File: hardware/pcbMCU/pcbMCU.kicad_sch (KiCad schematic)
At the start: 30 parts, among them J1 Conn_01x02, J2 Conn_01x04, J3 Conn_01x03, J4 Conn_01x05, SW1 SW_SPDT, U1 AMS1117-3.3, U2 AP62300, U3 ESP32-S3-WROOM-1

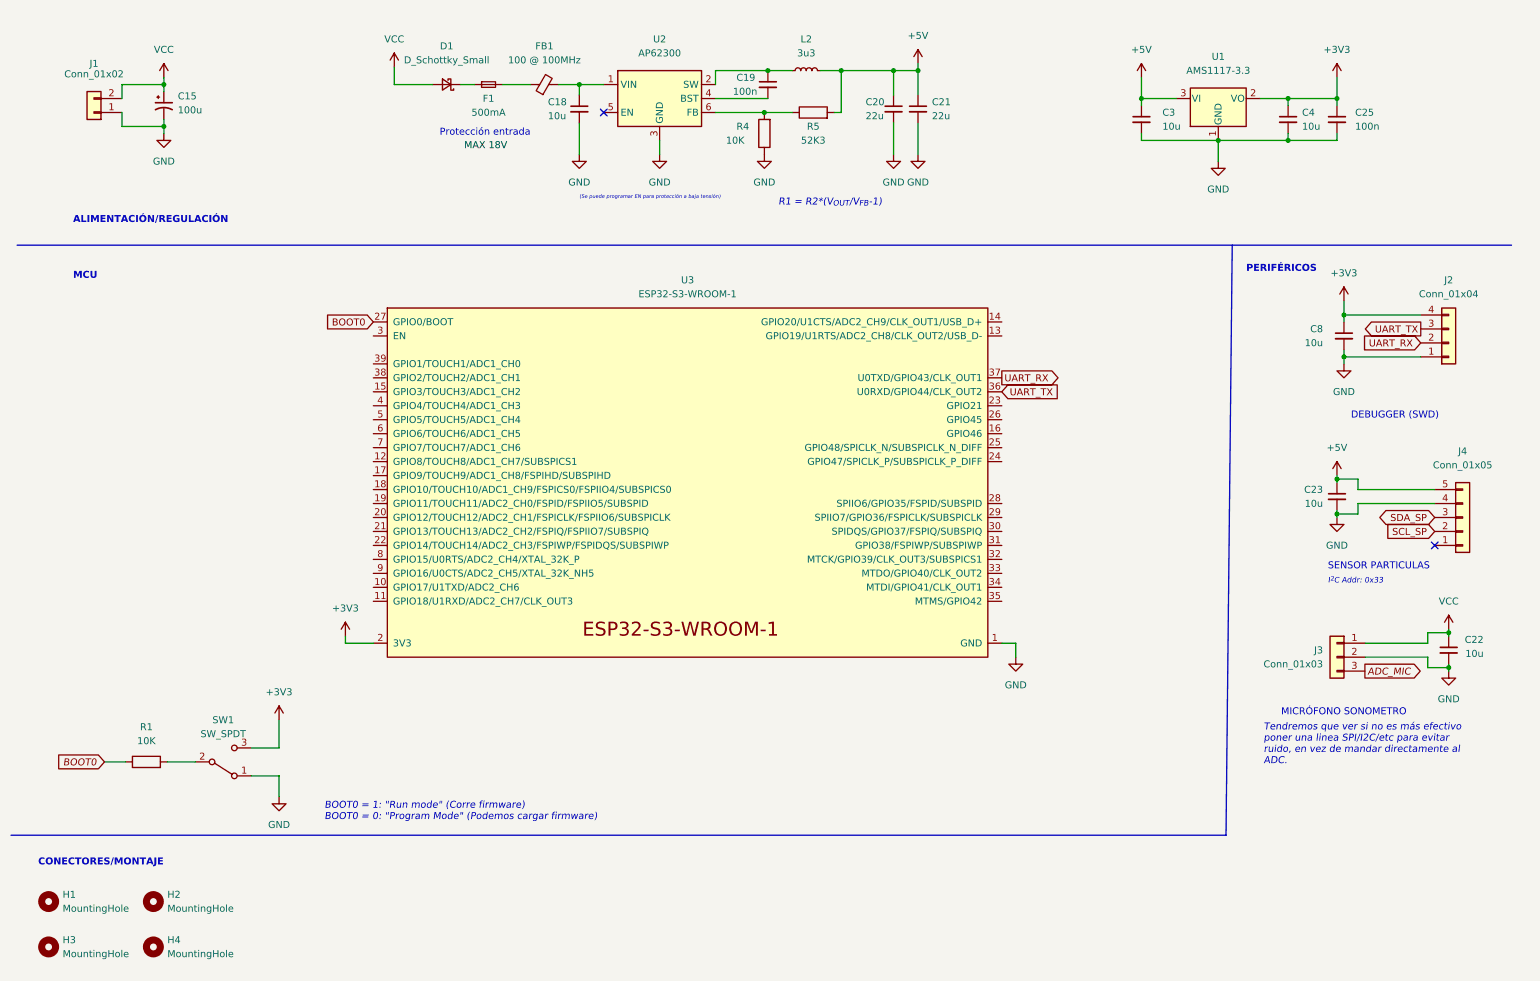
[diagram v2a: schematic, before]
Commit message: Esquema de PCB inicial, agrupación general de componentes
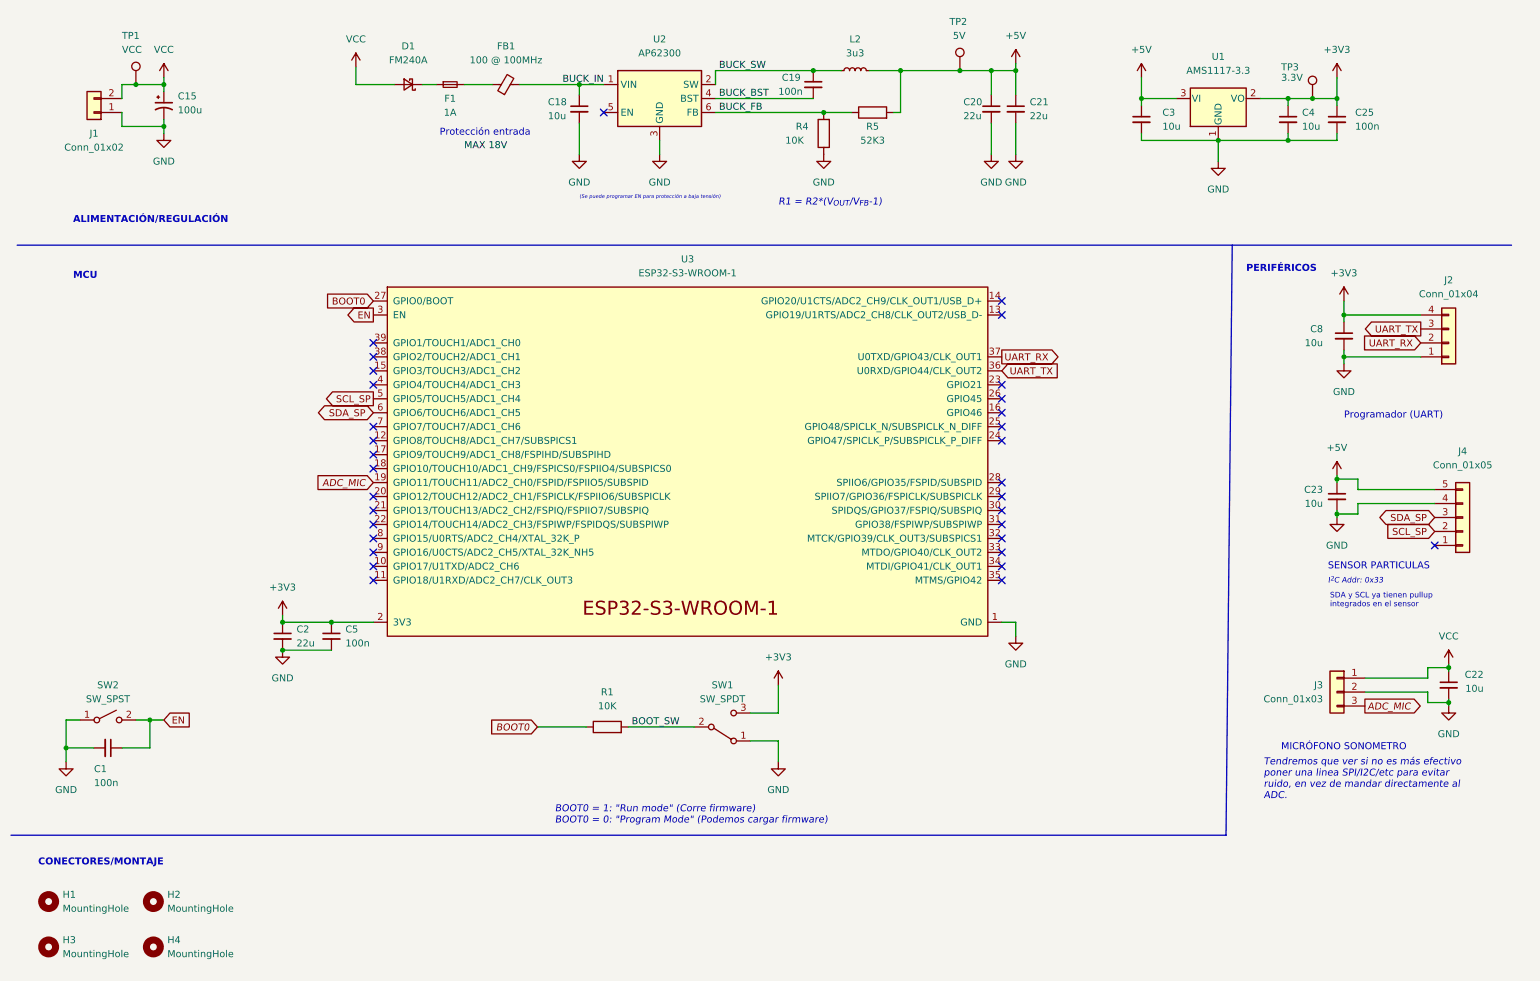
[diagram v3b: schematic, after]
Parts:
- added C1, C5: 100n, Capacitor_SMD:C_0603_1608Metric_Pad1.08x0.95mm_HandSolder, symbol Device:C_Small
- added C2: 22u, Capacitor_SMD:C_0603_1608Metric_Pad1.08x0.95mm_HandSolder, symbol Device:C_Small
- added SW2: SW_SPST, Button_Switch_THT:KSA_Tactile_SPST, symbol Switch:SW_SPST
- added TP1: VCC, TestPoint:TestPoint_Pad_D2.0mm, symbol Connector:TestPoint
- added TP2: 5V, TestPoint:TestPoint_Pad_D2.0mm, symbol Connector:TestPoint
- added TP3: 3.3V, TestPoint:TestPoint_Pad_D2.0mm, symbol Connector:TestPoint
- D1: value D_Schottky_Small -> FM240A; footprint Diode_SMD:D_0201_0603Metric_Pad0.64x0.40mm_HandSolder -> Diode_SMD:D_SMB
- F1: value 500mA -> 1A; footprint Fuse:Fuse_0603_1608Metric_Pad1.05x0.95mm_HandSolder -> Fuse:Fuse_1206_3216Metric_Pad1.42x1.75mm_HandSolder
- L2: footprint Inductor_SMD:L_0603_1608Metric_Pad1.05x0.95mm_HandSolder -> Inductor_SMD:L_0805_2012Metric_Pad1.15x1.40mm_HandSolder
- U3: footprint RF_Module:ESP32-S3-WROOM-1U -> Project Specific:ESP32-S3-WROOM-1U
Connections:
- net +3V3: now also C2.1, C5.1, TP3.1
- net +5V: now also TP2.1
- net ADC_MIC: now also U3.19 (GPIO11/TOUCH11/ADC2_CH0/FSPID/FSPIIO5/SUBSPID)
- net GND: now also C1.2, C2.2, C5.2, SW2.1 (A)
- net SCL_SP: now also U3.5 (GPIO5/TOUCH5/ADC1_CH4)
- net SDA_SP: now also U3.6 (GPIO6/TOUCH6/ADC1_CH5)
- net VCC: now also TP1.1
- net BUCK_SW: now reaches C19.1, L2.1, U2.2 (SW)
- net BOOT_SW: now reaches R1.2, SW1.2 (B)
- net BUCK_IN: now reaches C18.1, FB1.2, U2.1 (VIN)
- net BUCK_BST: now reaches C19.2, U2.4 (BST)
- net BUCK_FB: now reaches R4.2, R5.1, U2.6 (FB)
- net EN: now reaches U3.3 (EN)
- net EN: now also C1.1, SW2.2 (B)
- no-connect marks 2 -> 32
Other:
- note added: "Programador (UART)"
- note added: "SDA y SCL ya tienen pullup integrados en el sensor"
- note removed: "DEBUGGER (SWD)"
- moved on the sheet: C19, C20, C21, C22, D1, F1, FB1, J3, L2, R1, R4, R5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

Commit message: Añadido modelos 3D + Gráficos/descripciones
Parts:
- SW2: footprint Button_Switch_THT:KSA_Tactile_SPST -> Button_Switch_THT:SW_PUSH_6mm
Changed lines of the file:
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@@
     (property "Reference" "SW2" (id 0) (at 29.21 138.43 0))
     (property "Value" "SW_SPST" (id 1) (at 29.21 140.97 0))
-    (property "Footprint" "Button_Switch_THT:KSA_Tactile_SPST" (id 2) (at 29.21 144.78 0)
+    (property "Footprint" "Button_Switch_THT:SW_PUSH_6mm" (id 2) (at 29.21 144.78 0)
       (effects (font (size 1.27 1.27)) hide)
     )
@@
     )
     (path "/cad35490-a88a-4044-9eca-def0fda07e92"
-      (reference "SW2") (unit 1) (value "SW_SPST") (footprint "Button_Switch_THT:KSA_Tactile_SPST")
+      (reference "SW2") (unit 1) (value "SW_SPST") (footprint "Button_Switch_THT:SW_PUSH_6mm")
     )
     (path "/431c43c2-9246-47f0-9df2-20208297276e"
